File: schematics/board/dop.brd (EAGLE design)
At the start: 65.8 x 65.8 mm, 52 parts

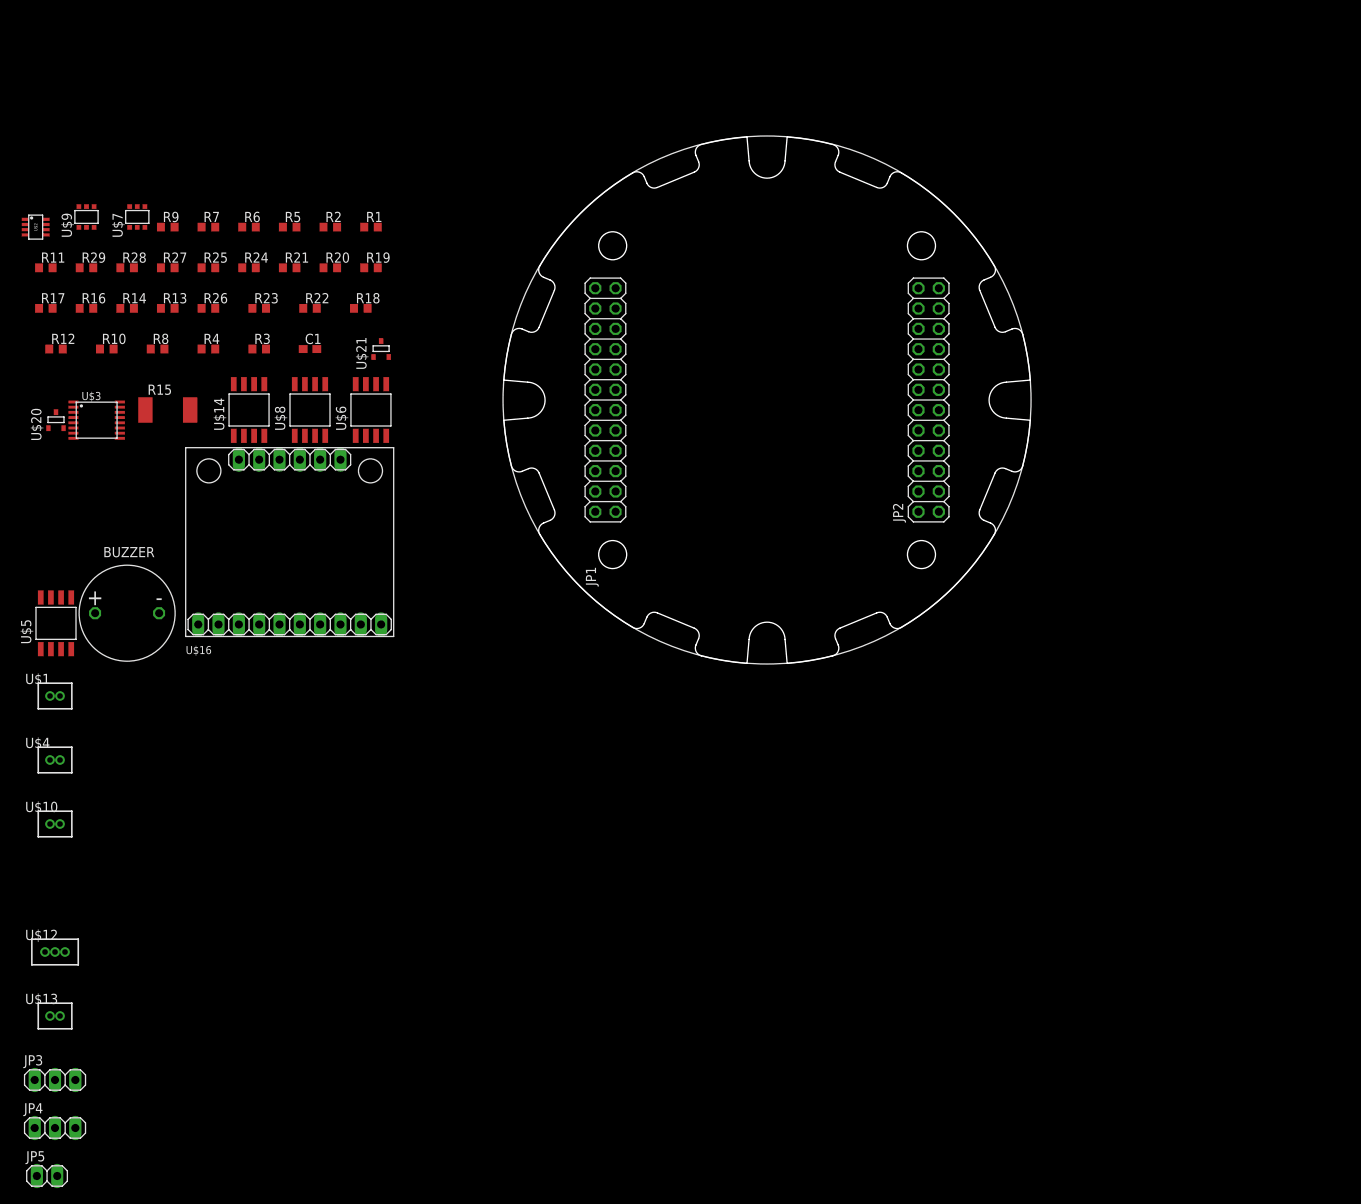
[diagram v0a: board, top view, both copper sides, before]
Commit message: добавил фоторезисторы на плату
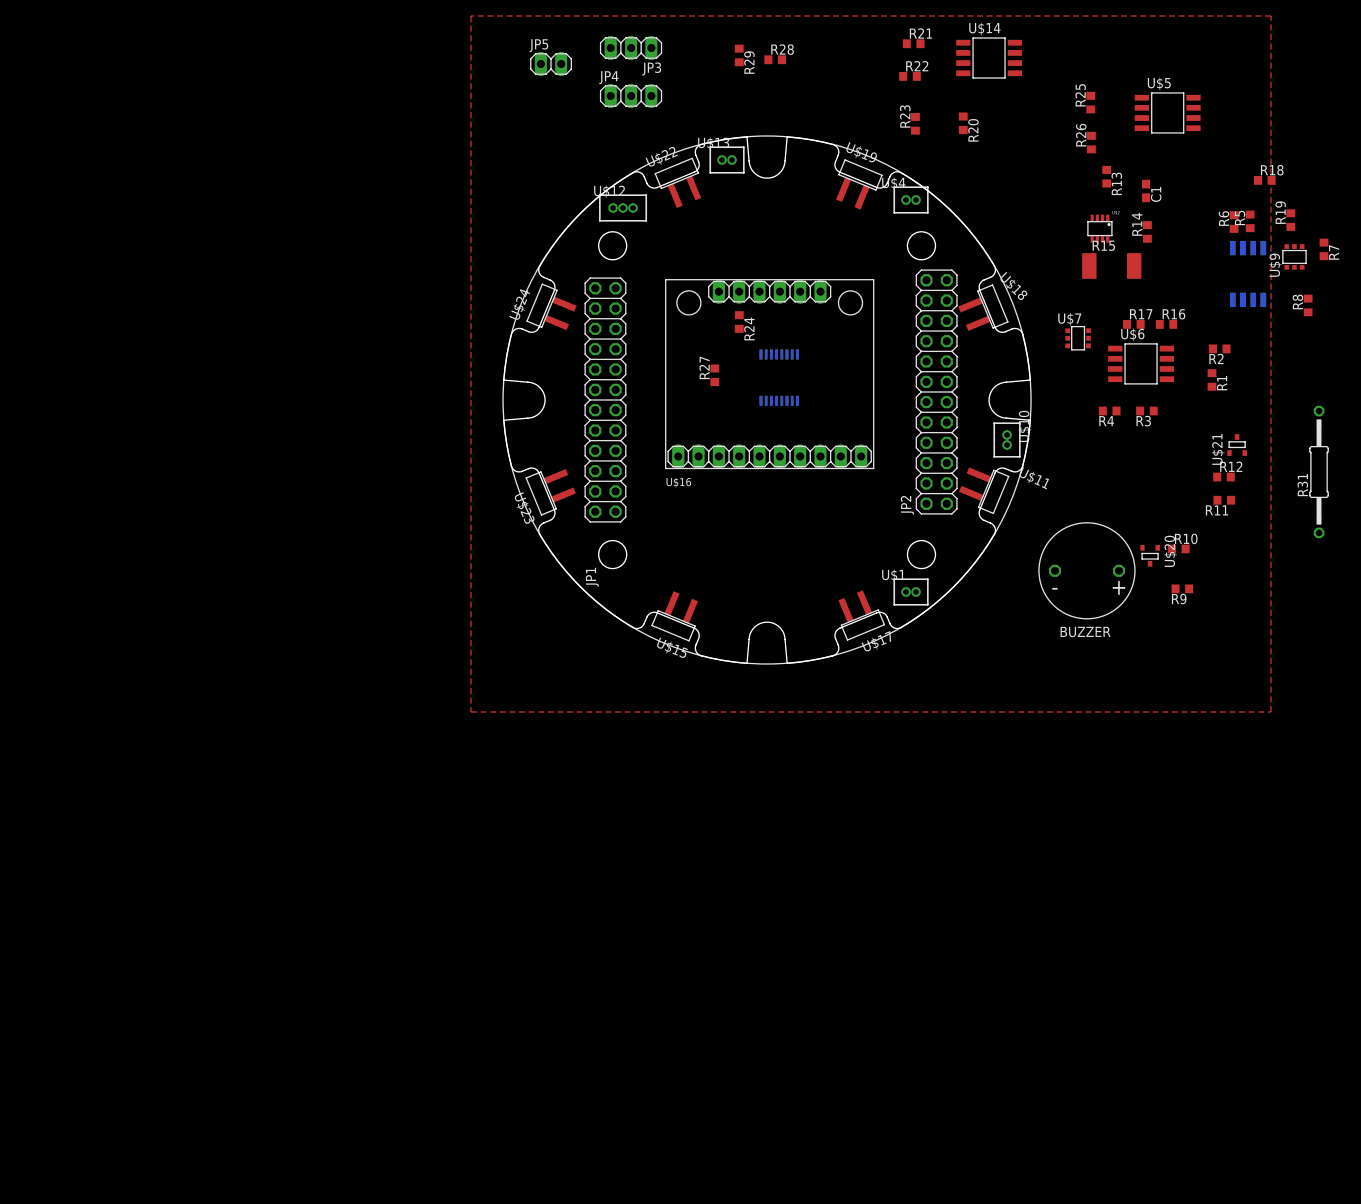
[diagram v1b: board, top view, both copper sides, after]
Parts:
- added R31: 100R, rcl:0207/15
- added U$11, U$15, U$17, U$18, U$19, U$22, U$23, U$24: VT93N1, CanCubeSat:VT93N1
- moved U$5 152.9 mm to (83.1, 68.9), turned to 270 degrees
- moved JP5 152.6 mm to (6.00, 75.0)
- moved U$9 151.1 mm to (98.9, 50.9)
- moved R11 150.1 mm to (90.2, 20.5), turned to 180 degrees
- moved JP3 147.7 mm to (16.0, 77.0), turned to 180 degrees
- moved JP4 147.7 mm to (16.0, 71.0)
- moved R12 146.9 mm to (90.1, 23.4)
- moved R8 143.9 mm to (100.6, 44.8), turned to 90 degrees
- moved R7 139.5 mm to (102.6, 51.8), turned to 270 degrees
- moved U$20 137.8 mm to (80.9, 13.5), turned to 180 degrees
- moved R10 136.3 mm to (84.5, 14.4)
- moved U$13 136.0 mm to (28.0, 63.0)
- moved R17 136.0 mm to (78.8, 42.5)
- moved R16 135.0 mm to (82.9, 42.5)
- moved R9 134.6 mm to (84.9, 9.39), turned to 180 degrees
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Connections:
- net N$39 renamed I2C
- net N$40 renamed ADC
- removed net CS: JP4.3
- removed net MOTOR_G: U$21.3
- removed net N$23: U$12.3
- removed net N$24: U$12.1
- removed net N$27: U$10.3
- removed net N$28: U$10.2
- removed net N$29: U$4.3
- removed net N$30: U$4.2
- removed net N$31: U$1.3
- removed net N$32: U$1.2
- removed net N$33: U$13.3
- removed net N$34: U$13.2
- new net MISO: JP2.17
- new net MOTOR3-: U$1.3, U$21.3
- new net PA4: JP2.21
- new net PA5: JP2.24
- new net PA6: JP1.22
- new net PA7: JP1.21
- new net PA8: JP1.4
- new net PC5: JP1.19
- new net SP-: R31.2, U$13.3
- new net VAB: JP1.15, JP2.10
- net 3V3: now also JP1.23, JP2.2
- net 5V: now also JP1.9, JP2.16
- net GND: now also JP1.10, JP1.16, JP1.2, JP1.24, JP2.1, JP2.15, JP2.23, JP2.9
- net INA_SP+: now also R31.1
- net LATCH: now also JP1.12, JP4.3
- net MOSI: now also JP2.18
- net MOTOR1+: now also U$10.2
- net MOTOR1-: now also U$10.3
- net MOTOR2+: now also U$4.2
- net MOTOR2-: now also U$4.3
- net PERE2: now also U$12.3
- net PERE3: now also U$12.1
- net SCK: now also JP2.14
- net SCL: now also JP2.8
- net SDA: now also JP2.7
- net SP+: now also U$13.2
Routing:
- added copper zone on layer 1, net GND

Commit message: я шпион спорадика, почти забацал плату доп
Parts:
- added R30, R32, R33, R34, R35, R36, R37, R38: 2k, rcl:R0603
- added U$25, U$26, U$27: JST_2CON, CanCubeSat:JST_2CON_1.25
- R31: device rcl:0207/15 -> CanCubeSat:0207/15
- U$2: device CanCubeSat:SOT23-8 -> CanCubeSat:INA219AID
- U$20, U$21: device CanCubeSat:SOT23-3 -> CanCubeSat:SI2302CDS
- U$3: device CanCubeSat:TSSOP16 -> CanCubeSat:74HC595
- moved R7 73.5 mm to (29.3, 46.3), turned to 0 degrees
- moved R19 71.3 mm to (28.7, 40.9), turned to 0 degrees
- moved U$8 70.8 mm to (22.6, 42.6), flipped to the top, turned to 90 degrees
- moved U$9 70.2 mm to (29.1, 43.6), turned to 90 degrees
- moved R8 68.7 mm to (32.0, 45.9), turned to 270 degrees
- moved R5 68.5 mm to (27.0, 38.7), turned to 180 degrees
- moved R18 66.1 mm to (31.9, 41.4), turned to 90 degrees
- moved R6 66.0 mm to (26.1, 46.3), turned to 180 degrees
- moved R12 65.4 mm to (33.8, 56.7), turned to 90 degrees
- moved R11 65.1 mm to (36.0, 56.6), turned to 270 degrees
- moved R1 62.7 mm to (28.7, 54.0), turned to 0 degrees
- moved R16 62.3 mm to (20.7, 46.4)
- moved R2 61.6 mm to (28.7, 48.6), turned to 0 degrees
- moved R31 60.9 mm to (41.8, 14.8), turned to 0 degrees
- moved U$21 60.8 mm to (38.6, 56.7), turned to 270 degrees
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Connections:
- net 3V3: now also R30.2, R32.2, R33.2, R34.2, R35.2, R36.2, R37.2, R38.2
- net FOTO1: now also R32.1, U$17.P$2
- net FOTO2: now also R34.1, U$11.P$2
- net FOTO3: now also R30.1, U$18.P$1
- net FOTO4: now also R35.1, U$19.P$1
- net FOTO5: now also R36.1, U$22.P$1
- net FOTO6: now also R38.1, U$24.P$1
- net FOTO7: now also R37.1, U$23.P$1
- net FOTO8: now also R33.1, U$15.P$2
- net GND: now also U$11.P$1, U$15.P$1, U$17.P$1, U$18.P$2, U$19.P$2, U$22.P$2, U$23.P$2, U$24.P$2
- net PERE1_G: now also U$25.2
- net PERE2_G: now also U$26.2
- net PERE3_G: now also U$27.2
- net VAB: now also U$25.3, U$26.3, U$27.3
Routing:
- net 3V3: track 0.00 -> 211.5 mm, vias 0 -> 12
- net GND: track 0.00 -> 186.6 mm, vias 0 -> 8
- net FOTO5: track 0.00 -> 57.7 mm, vias 0 -> 2
- net FOTO4: track 0.00 -> 54.6 mm, vias 0 -> 2
- net FOTO3: track 0.00 -> 48.4 mm, vias 0 -> 2
- net FOTO6: track 0.00 -> 44.9 mm
- net LATCH: track 0.00 -> 40.5 mm, vias 0 -> 1
- net SCL: track 0.00 -> 32.6 mm
- net SDA: track 0.00 -> 31.8 mm
- net 5V: track 0.00 -> 30.3 mm, vias 0 -> 5
- net PERE2_G: track 0.00 -> 28.4 mm
- net PERE1_G: track 0.00 -> 27.8 mm
- net FOTO2: track 0.00 -> 27.0 mm
- net MOTOR1-: track 0.00 -> 24.1 mm, vias 0 -> 2
- net FOTO7: track 0.00 -> 23.2 mm
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
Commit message: Создали stl нижней части
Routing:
- net FOTO8: track 6.09 -> 4.67 mm
- net GND: track 186.6 -> 187.6 mm
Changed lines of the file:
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@@
 <?xml version="1.0" encoding="utf-8"?>
 <!DOCTYPE eagle SYSTEM "eagle.dtd">
-<eagle version="9.6.2">
+<eagle version="9.4.2">
 <drawing>
 <settings>
-<setting alwaysvectorfont="no"/>
+<setting alwaysvectorfont="yes"/>
 <setting verticaltext="up"/>
 </settings>
@@
 <wire x1="34.605" y1="24.605" x2="36.59461875" y2="24.605" width="0.25" layer="16"/>
 <wire x1="28.68" y1="18.68" x2="34.605" y2="24.605" width="0.25" layer="16"/>
-<wire x1="9.4548375" y1="21.1051625" x2="11.53" y2="19.03" width="0.25" layer="1"/>
-<wire x1="9.4548375" y1="21.902315625" x2="9.4548375" y2="21.1051625" width="0.25" layer="1"/>
-<wire x1="6.6074625" y1="23.428871875" x2="7.92828125" y2="23.428871875" width="0.25" layer="1"/>
-<wire x1="7.92828125" y1="23.428871875" x2="9.4548375" y2="21.902315625" width="0.25" layer="1"/>
+<wire x1="10.0548375" y1="20.5051625" x2="11.53" y2="19.03" width="0.25" layer="1"/>
+<wire x1="10.0548375" y1="21.902315625" x2="10.0548375" y2="20.5051625" width="0.25" layer="1"/>
+<wire x1="8.12828125" y1="23.828871875" x2="7.0074625" y2="23.828871875" width="0.25" layer="1"/>
+<wire x1="6.6074625" y1="23.428871875" x2="7.0074625" y2="23.828871875" width="0.25" layer="1"/>
+<wire x1="8.12828125" y1="23.828871875" x2="10.0548375" y2="21.902315625" width="0.25" layer="1"/>
 <wire x1="7.664171875" y1="44.980821875" x2="7.664171875" y2="43.546325" width="0.25" layer="1"/>
 <wire x1="7.664171875" y1="43.546325" x2="8.59813125" y2="42.612365625" width="0.25" layer="1"/>
@@
 <wire x1="45.1" y1="11.9" x2="43.4" y2="13.6" width="0.25" layer="16"/>
 <wire x1="43.4" y1="13.6" x2="35.4" y2="13.6" width="0.25" layer="16"/>
-<wire x1="23.428871875" y1="6.6074625" x2="24.221409375" y2="7.4" width="0.25" layer="1"/>
-<wire x1="24.221409375" y1="7.4" x2="38.9468" y2="7.4" width="0.25" layer="1"/>
+<wire x1="23.821409375" y1="7.4" x2="23.428871875" y2="7.0074625" width="0.25" layer="1"/>
+<wire x1="23.428871875" y1="6.6074625" x2="23.428871875" y2="7.0074625" width="0.25" layer="1"/>
+<wire x1="23.821409375" y1="7.4" x2="38.9468" y2="7.4" width="0.25" layer="1"/>
 <via x="38.9468" y="7.4" extent="1-16" drill="0.35"/>
 <wire x1="38.9468" y1="7.4" x2="39.2968" y2="7.75" width="0.25" layer="16"/>
@@
 <contactref element="R37" pad="1"/>
 <contactref element="U$23" pad="P$1"/>
-<wire x1="24.78" y1="10.94" x2="24.53925625" y2="10.94" width="0.25" layer="1"/>
-<wire x1="12.8745375" y1="15.808809375" x2="8.441671875" y2="20.241675" width="0.25" layer="1"/>
-<wire x1="8.441671875" y1="20.241675" x2="7.564171875" y2="21.119175" width="0.25" layer="1"/>
-<wire x1="24.53925625" y1="10.94" x2="19.670446875" y2="15.808809375" width="0.25" layer="1"/>
-<wire x1="19.670446875" y1="15.808809375" x2="12.8745375" y2="15.808809375" width="0.25" layer="1"/>
-<wire x1="7.8" y1="18.75" x2="7.8" y2="19.600003125" width="0.25" layer="1"/>
-<wire x1="7.8" y1="19.600003125" x2="8.441671875" y2="20.241675" width="0.25" layer="1"/>
+<wire x1="24.78" y1="11.94" x2="24.78" y2="10.94" width="0.25" layer="1"/>
+<wire x1="24.78" y1="11.94" x2="23.58" y2="13.14" width="0.25" layer="1"/>
+<wire x1="23.58" y1="13.14" x2="22.33925625" y2="13.14" width="0.25" layer="1"/>
+<wire x1="11.6745375" y1="16.008809375" x2="8.933346875" y2="18.75" width="0.25" layer="1"/>
+<wire x1="22.33925625" y1="13.14" x2="19.470446875" y2="16.008809375" width="0.25" layer="1"/>
+<wire x1="19.470446875" y1="16.008809375" x2="11.6745375" y2="16.008809375" width="0.25" layer="1"/>
+<wire x1="7.8" y1="18.75" x2="7.8" y2="20.883346875" width="0.25" layer="1"/>
+<wire x1="7.8" y1="20.883346875" x2="7.564171875" y2="21.119175" width="0.25" layer="1"/>
+<wire x1="7.8" y1="18.75" x2="8.933346875" y2="18.75" width="0.25" layer="1"/>
 </signal>
 <signal name="FOTO8">
@@
 <contactref element="R33" pad="1"/>
 <contactref element="U$15" pad="P$2"/>
-<wire x1="21.119175" y1="7.564171875" x2="21.377503125" y2="7.8225" width="0.25" layer="1"/>
-<wire x1="21.377503125" y1="7.8225" x2="22.24" y2="8.684996875" width="0.25" layer="1"/>
-<wire x1="22.24" y1="8.684996875" x2="22.24" y2="10.94" width="0.25" layer="1"/>
-<wire x1="19.45" y1="8.6" x2="20.600003125" y2="8.6" width="0.25" layer="1"/>
-<wire x1="20.600003125" y1="8.6" x2="21.377503125" y2="7.8225" width="0.25" layer="1"/>
+<wire x1="21.355003125" y1="8.6" x2="22.24" y2="9.484996875" width="0.25" layer="1"/>
+<wire x1="22.24" y1="9.484996875" x2="22.24" y2="10.94" width="0.25" layer="1"/>
+<wire x1="19.45" y1="8.6" x2="21.355003125" y2="8.6" width="0.25" layer="1"/>
+<wire x1="21.077503125" y1="7.5225" x2="21.119175" y2="7.564171875" width="0.25" layer="1"/>
 </signal>
 <signal name="PERE1">
